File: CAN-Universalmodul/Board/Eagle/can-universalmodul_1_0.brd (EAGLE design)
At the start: 74 x 50 mm, 42 parts, among them IC1 MCP 2562, IC2 MCP 2515, IC3 ATMEGA 328P, Q1 16M, Q2 16M, X1 MINI-USB-UX60-MB-5ST

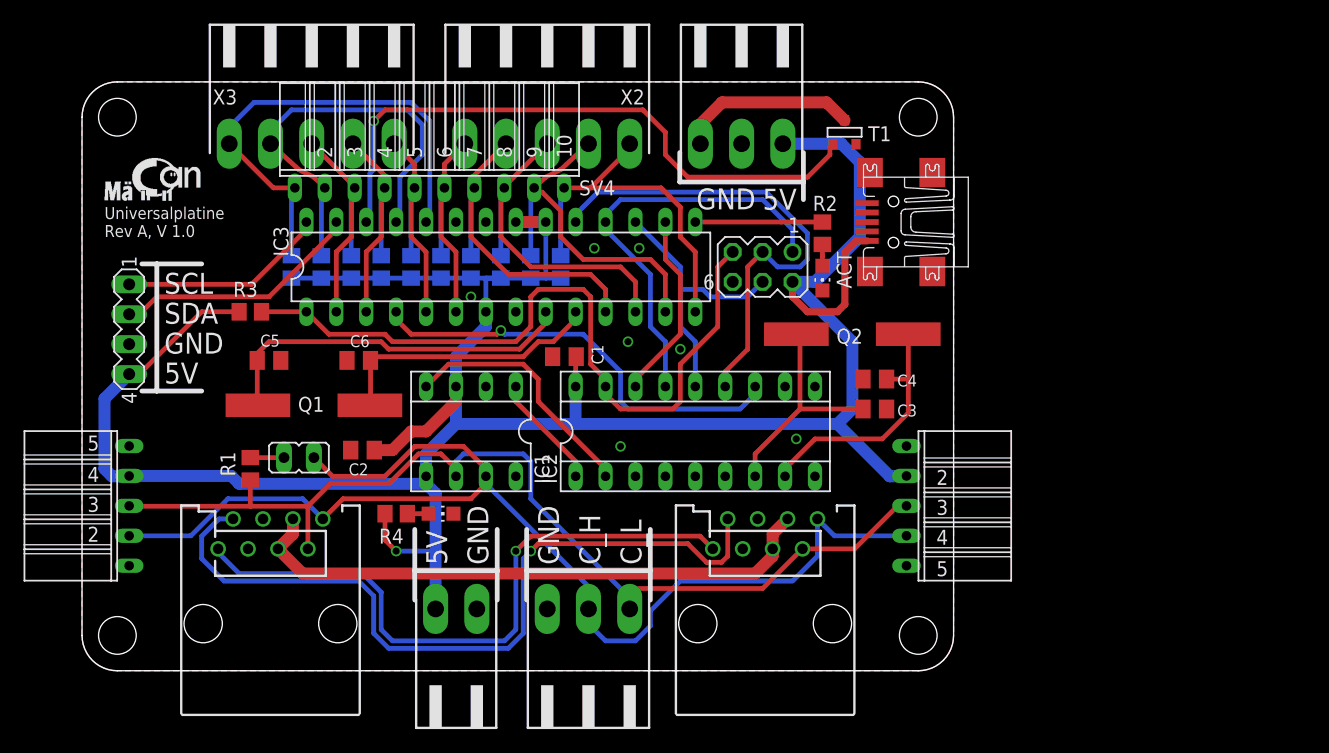
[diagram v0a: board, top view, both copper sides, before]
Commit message: I²C-Anschluss gedreht, Namensschema geändert.
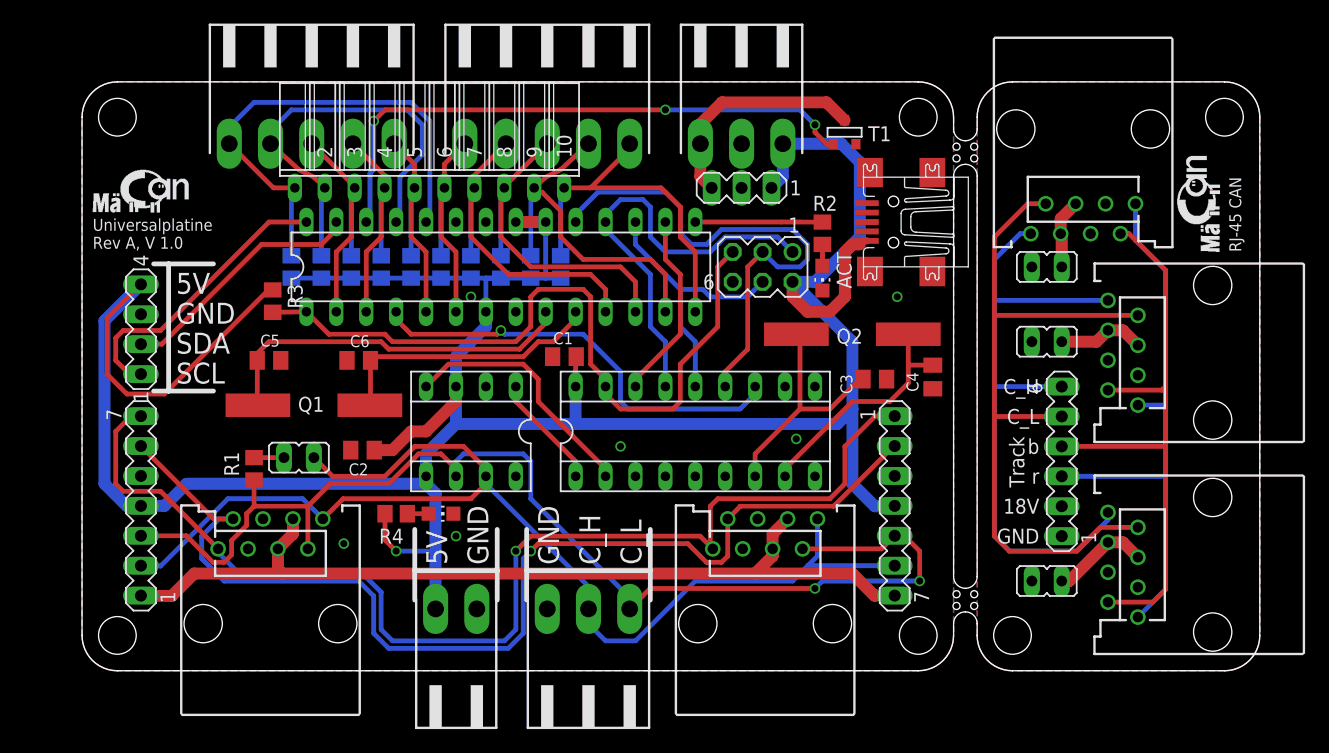
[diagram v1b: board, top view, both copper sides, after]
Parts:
- removed SV3: (no value), con-lsta:FE05W
- added J3, J4, J5: (no value), con-amp:215877-7
- added JP2, JP3, JP4: (no value), jumper:JP1
- added SV5: (no value), con-lstb:MA06-1
- added SV6, SV7: (no value), con-lstb:MA07-1
- SV2: device con-lsta:FE05W -> con-lstb:MA03-1
- moved SV2 58.6 mm to (56.0, 41.0), turned to 180 degrees
- moved C4 4.93 mm to (72.2, 24.9), turned to 90 degrees
- moved C3 2.54 mm to (67.3, 24.8)
- moved R3 2.11 mm to (16.2, 31.4), turned to 90 degrees
- moved SV8 1.00 mm to (5.00, 29.0), turned to 90 degrees
- moved R1 0.32 mm to (14.6, 17.1)
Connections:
- removed net N$32: J1.1, J2.1
- new net 18V: J1.5, J1.6, J2.5, J2.6, SV6.1, SV7.7
- new net BR: J1.2, J2.2, SV6.6, SV7.2
- new net N$10: J3.5, J3.6, JP2.1
- new net N$11: J3.1, J4.1, J5.1, SV5.3
- new net N$14: J3.2, J4.2, J5.2, SV5.4
- new net N$15: J3.7, J4.7, J5.7, SV5.5
- new net N$16: J3.8, J4.8, J5.8, SV5.6
- new net RT: J1.1, J2.1, SV6.7, SV7.1
- new net _18V: JP2.2, JP3.2, JP4.2, SV5.2
- new net _GND: J3.3, J3.4, J4.3, J4.4, J5.3, J5.4, SV5.1
- net CAN-H: now also SV6.2, SV7.6; no longer SV2.2, SV3.4
- net CAN-L: now also SV6.3, SV7.5; no longer SV2.3, SV3.3
- net GND: now also SV2.2, SV6.5, SV7.3; no longer SV2.1, SV2.5, SV3.1, SV3.5
- net N$1: now also J5.5, J5.6, JP4.1; no longer J1.5, J1.6, J2.5, J2.6
- net N$22: now also SV2.3
- net N$3: now also J4.5, J4.6, JP3.1; no longer J1.2, J2.2
- net VCC: now also SV2.1, SV6.4, SV7.4; no longer SV2.4, SV3.2
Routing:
- net RT: track 0.00 -> 97.8 mm, vias 0 -> 1
- net BR: track 0.00 -> 93.4 mm, vias 0 -> 1
- net 18V: track 0.00 -> 76.7 mm
- net N$15: track 0.00 -> 62.4 mm
- net N$3: track 66.3 -> 8.35 mm, vias 1 -> 0
- net N$32: track 55.3 -> 0.00 mm, vias 1 -> 0
- net N$16: track 0.00 -> 54.7 mm
- net N$14: track 0.00 -> 51.4 mm
- net N$11: track 0.00 -> 48.3 mm
- net N$1: track 50.2 -> 7.39 mm
- net VCC: track 222.3 -> 255.2 mm
- net CAN-L: track 89.1 -> 103.0 mm, vias 0 -> 2
- net N$33: track 17.6 -> 24.8 mm
- net N$10: track 0.00 -> 5.92 mm
- net N$22: track 15.3 -> 19.5 mm
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- added copper zone on layer 1, net _18V
- added copper zone on layer 16, net _GND
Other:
- board size 74 x 50 mm -> 100 x 50 mm
- board text added: "18V"
- board text added: "RJ-45 CAN"
- board text added: "Track"
- board text added: "b"
- board text added: "r"

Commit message: Stecker hinzugefügt
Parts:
- added X4: B4B-ZR, con-jst:B4B-ZR
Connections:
- net N$15: now also X4.3
- net N$16: now also X4.2
- net _18V: now also X4.1
- net _GND: now also X4.4
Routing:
- net N$16: track 54.7 -> 72.7 mm
- net N$15: track 62.4 -> 76.9 mm

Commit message: Anpassungen
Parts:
- added SV3: Serial, con-lstb:MA04-1
- moved C6 10.2 mm to (19.1, 17.1), turned to 90 degrees
- moved C5 9.23 mm to (16.5, 17.1), turned to 90 degrees
- moved JP1 8.63 mm to (9.84, 19.1), turned to 0 degrees
- moved R1 1.42 mm to (13.3, 17.8), turned to 180 degrees
- moved C1 1.27 mm to (42.2, 26.7)
- moved C2 0.71 mm to (24.1, 18.1)
- moved Q1 0.64 mm to (19.7, 21.9)
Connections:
- net 7: now also SV3.3
- net 8: now also SV3.2
- net GND: now also SV3.4
- net RESET: now also SV3.1
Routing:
- net CAN-H: track 101.7 -> 109.2 mm, vias 0 -> 1
- net RESET: track 62.1 -> 68.9 mm
- net N$8: track 23.9 -> 28.5 mm
- net 8: track 22.3 -> 26.5 mm
- net 7: track 21.9 -> 26.1 mm
- net CAN-L: track 103.0 -> 105.0 mm
- net 18V: track 76.7 -> 77.8 mm
- net VCC: track 255.2 -> 256.1 mm
- net N$7: track 32.0 -> 32.7 mm
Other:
- board text added: "Rs Rx Tx GND"

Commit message: PCB-Production-Ready
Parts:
- removed R10, R11, R12, R13, R14, R5, R6, R7, R8, R9: 10k, rcl:R0805
- removed SV3: Serial, con-lstb:MA04-1
- added C7: 100n, rcl:C0805K
- added J6: FTDI_BASICPTH, SparkFun-Connectors:FTDI_BASIC
- moved R4 46.3 mm to (63.8, 41.0), flipped to the bottom, turned to 90 degrees
- moved PWR 41.2 mm to (63.2, 38.4), turned to 90 degrees
- moved ACT 7.31 mm to (63.2, 40.6), turned to 270 degrees
- moved R2 4.02 mm to (61.6, 41.0), flipped to the bottom, turned to 270 degrees
- moved R3 3.48 mm to (17.5, 34.6), flipped to the bottom, turned to 0 degrees
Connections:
- new net N$17: C7.2, J6.DTR
- net 1: no longer R5.1
- net 10: no longer R14.1
- net 2: no longer R6.1
- net 3: no longer R7.1
- net 4: no longer R8.1
- net 5: no longer R9.1
- net 6: no longer R10.1
- net 7: now also J6.RXI; no longer R11.1, SV3.3
- net 8: now also J6.TXO; no longer R12.1, SV3.2
- net 9: no longer R13.1
- net GND: now also J6.GND; no longer SV3.4
- net RESET: now also C7.1; no longer SV3.1
- net VCC: no longer R10.2, R11.2, R12.2, R13.2, R14.2, R5.2, R6.2, R7.2, R8.2, R9.2
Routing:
- net VCC: track 256.1 -> 209.7 mm, vias 1 -> 0
- net 3: track 31.0 -> 24.2 mm
- net 1: track 31.0 -> 24.2 mm
- net 8: track 26.5 -> 20.0 mm
- net 7: track 26.1 -> 19.6 mm
- net 4: track 30.2 -> 23.8 mm
- net 9: track 36.4 -> 30.9 mm
- net 10: track 41.7 -> 36.2 mm
- net 6: track 21.5 -> 16.0 mm
- net 5: track 21.5 -> 16.0 mm
- net 2: track 30.5 -> 25.3 mm
- net N$17: track 0.00 -> 4.61 mm
- net INT: track 37.2 -> 41.3 mm, vias 1 -> 0
- net RESET: track 68.9 -> 72.5 mm, vias 0 -> 1
- net RT: track 97.8 -> 94.7 mm
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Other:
- board text removed: "Rs Rx Tx GND"
